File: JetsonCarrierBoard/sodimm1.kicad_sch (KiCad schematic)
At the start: 6 parts

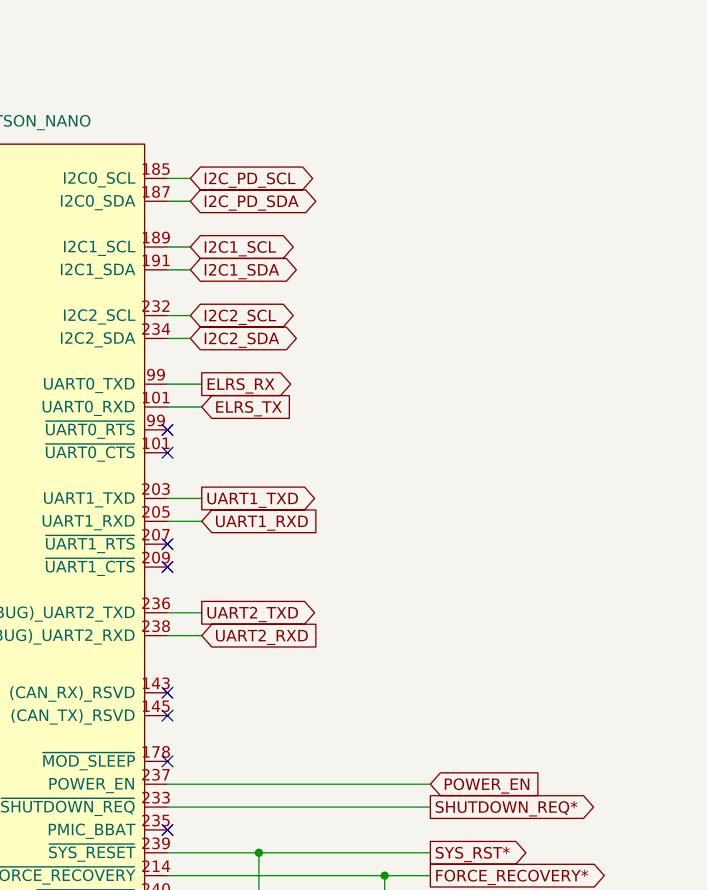
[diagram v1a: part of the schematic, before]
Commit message: Added basic circuits, LED circuit, GPIO pins in GPIO page
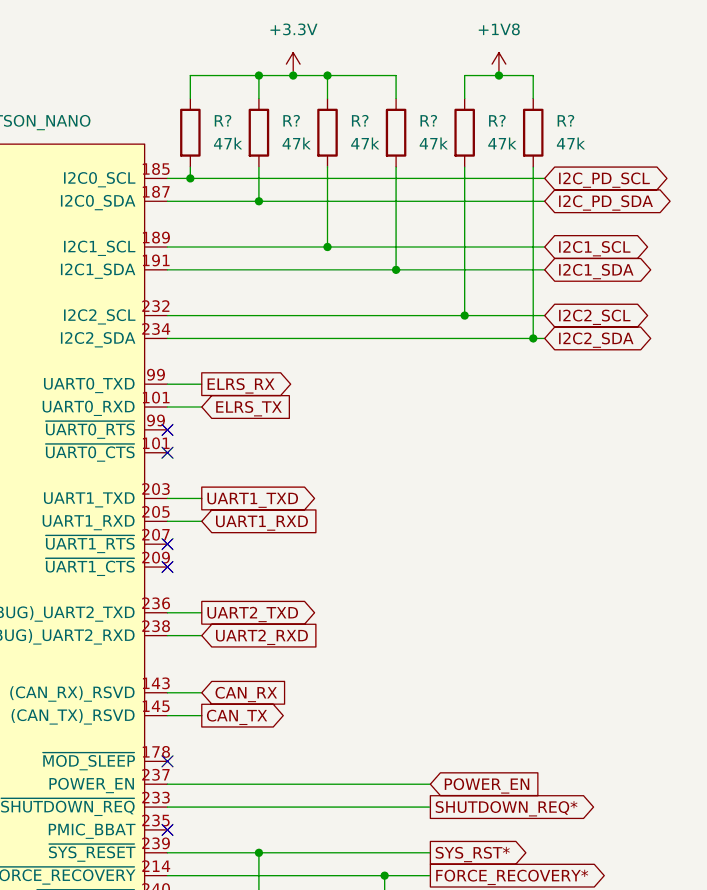
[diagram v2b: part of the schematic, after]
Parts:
- added R? (x6): 47k, symbol Device:R
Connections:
- net I2C1_SCL: now also R?.2
- net I2C1_SDA: now also R?.2
- net I2C2_SCL: now also R?.2
- net I2C2_SDA: now also R?.2
- net I2C_PD_SCL: now also R?.2
- net I2C_PD_SDA: now also R?.2
- net CAN_RX: now reaches J?.143 ((CAN_RX)_RSVD)
- net CAN_TX: now reaches J?.145 ((CAN_TX)_RSVD)
- new net +1V8: R?.1, R?.1
- new net +3.3V: R?.1, R?.1, R?.1, R?.1
- no-connect marks 9 -> 7

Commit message: GPIO wiring
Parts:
- removed R? (x2): 47k, symbol Device:R
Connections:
- net I2C2_SCL: no longer names the net of J?.232 (I2C2_SCL)
- net I2C2_SDA: no longer names the net of J?.234 (I2C2_SDA)
- no-connect marks 7 -> 9
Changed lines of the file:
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@@
   (junction (at 119.38 109.22) (diameter 0) (color 0 0 0 0)
   )
-  (junction (at 204.47 21.59) (diameter 0) (color 0 0 0 0)
-  )
   (junction (at 119.38 43.18) (diameter 0) (color 0 0 0 0)
   )
@@
   )
   (junction (at 119.38 129.54) (diameter 0) (color 0 0 0 0)
-  )
-  (junction (at 200.66 48.26) (diameter 0) (color 0 0 0 0)
-  )
-  (junction (at 208.28 50.8) (diameter 0) (color 0 0 0 0)
   )
   (junction (at 119.38 114.3) (diameter 0) (color 0 0 0 0)
@@
   (no_connect (at 167.64 63.5))
   (no_connect (at 167.64 60.96))
+  (no_connect (at 167.64 50.8))
+  (no_connect (at 167.64 48.26))
   (no_connect (at 167.64 113.03))
   (wire (pts (xy 119.38 124.46) (xy 119.38 127))
@@
     (stroke (width 0) (type default) (color 0 0 0 0))
   )
-  (wire (pts (xy 200.66 24.13) (xy 200.66 21.59))
-    (stroke (width 0) (type default) (color 0 0 0 0))
-  )
   (wire (pts (xy 167.64 55.88) (xy 171.45 55.88))
     (stroke (width 0) (type default) (color 0 0 0 0))
@@
     (stroke (width 0) (type default) (color 0 0 0 0))
   )
-  (wire (pts (xy 208.28 50.8) (xy 208.28 31.75))
-    (stroke (width 0) (type default) (color 0 0 0 0))
-  )
   (wire (pts (xy 119.38 38.1) (xy 119.38 40.64))
     (stroke (width 0) (type default) (color 0 0 0 0))
@@
     (stroke (width 0) (type default) (color 0 0 0 0))
   )
-  (wire (pts (xy 167.64 50.8) (xy 208.28 50.8))
-    (stroke (width 0) (type default) (color 0 0 0 0))
-  )
   (wire (pts (xy 170.18 121.92) (xy 170.18 124.46))
     (stroke (width 0) (type default) (color 0 0 0 0))
@@
     (stroke (width 0) (type default) (color 0 0 0 0))
   )
-  (wire (pts (xy 204.47 21.59) (xy 208.28 21.59))
-    (stroke (width 0) (type default) (color 0 0 0 0))
-  )
   (wire (pts (xy 119.38 147.32) (xy 121.92 147.32))
     (stroke (width 0) (type default) (color 0 0 0 0))
@@
     (stroke (width 0) (type default) (color 0 0 0 0))
   )
-  (wire (pts (xy 167.64 48.26) (xy 200.66 48.26))
-    (stroke (width 0) (type default) (color 0 0 0 0))
-  )
   (wire (pts (xy 119.38 50.8) (xy 119.38 53.34))
     (stroke (width 0) (type default) (color 0 0 0 0))
@@
     (stroke (width 0) (type default) (color 0 0 0 0))
   )
-  (wire (pts (xy 200.66 21.59) (xy 204.47 21.59))
-    (stroke (width 0) (type default) (color 0 0 0 0))
-  )
   (wire (pts (xy 170.18 154.94) (xy 170.18 157.48))
     (stroke (width 0) (type default) (color 0 0 0 0))
@@
     (stroke (width 0) (type default) (color 0 0 0 0))
   )
-  (wire (pts (xy 208.28 21.59) (xy 208.28 24.13))
-    (stroke (width 0) (type default) (color 0 0 0 0))
-  )
   (wire (pts (xy 177.8 35.56) (xy 177.8 31.75))
     (stroke (width 0) (type default) (color 0 0 0 0))
@@
     (stroke (width 0) (type default) (color 0 0 0 0))
   )
-  (wire (pts (xy 200.66 48.26) (xy 200.66 31.75))
-    (stroke (width 0) (type default) (color 0 0 0 0))
-  )
   (wire (pts (xy 119.38 68.58) (xy 119.38 71.12))
     (stroke (width 0) (type default) (color 0 0 0 0))
@@
     (stroke (width 0) (type default) (color 0 0 0 0))
   )
-  (wire (pts (xy 200.66 48.26) (xy 209.55 48.26))
-    (stroke (width 0) (type default) (color 0 0 0 0))
-  )
   (wire (pts (xy 167.64 90.17) (xy 171.45 90.17))
     (stroke (width 0) (type default) (color 0 0 0 0))
@@
     (stroke (width 0) (type default) (color 0 0 0 0))
   )
-  (wire (pts (xy 208.28 50.8) (xy 209.55 50.8))
-    (stroke (width 0) (type default) (color 0 0 0 0))
-  )
   (wire (pts (xy 119.38 134.62) (xy 119.38 137.16))
     (stroke (width 0) (type default) (color 0 0 0 0))
@@
     (effects (font (size 1.27 1.27)) (justify left))
     (property "Intersheet References" "${INTERSHEET_REFS}" (id 0) (at 215.1683 102.7906 0)
-      (effects (font (size 1.27 1.27)) (justify left) hide)
-    )
-  )
-  (global_label "I2C2_SCL" (shape bidirectional) (at 209.55 48.26 0) (fields_autoplaced)
-    (effects (font (size 1.27 1.27)) (justify left))
-    (property "Intersheet References" "${INTERSHEET_REFS}" (id 0) (at 220.7321 48.1806 0)
-      (effects (font (size 1.27 1.27)) (justify left) hide)
-    )
-  )
-  (global_label "I2C2_SDA" (shape bidirectional) (at 209.55 50.8 0) (fields_autoplaced)
-    (effects (font (size 1.27 1.27)) (justify left))
-    (property "Intersheet References" "${INTERSHEET_REFS}" (id 0) (at 220.7926 50.7206 0)
       (effects (font (size 1.27 1.27)) (justify left) hide)
     )
@@
     )
     (pin "1")
-  )
-  (symbol (lib_id "Device:R") (at 208.28 27.94 0) (unit 1)
-    (in_bom yes) (on_board yes) (fields_autoplaced)
-    (property "Reference" "R?" (id 0) (at 210.82 26.6699 0)
-      (effects (font (size 1.27 1.27)) (justify left))
-    )
-    (property "Value" "47k" (id 1) (at 210.82 29.2099 0)
-      (effects (font (size 1.27 1.27)) (justify left))
-    )
-    (property "Footprint" "" (id 2) (at 206.502 27.94 90)
-      (effects (font (size 1.27 1.27)) hide)
-    )
-    (property "Datasheet" "~" (id 3) (at 208.28 27.94 0)
-      (effects (font (size 1.27 1.27)) hide)
-    )
-    (pin "1")
-    (pin "2")
   )
   (symbol (lib_id "Device:D_TVS") (at 191.77 120.65 90) (unit 1)
@@
     (pin "2")
   )
-  (symbol (lib_id "Device:R") (at 200.66 27.94 0) (unit 1)
-    (in_bom yes) (on_board yes) (fields_autoplaced)
-    (property "Reference" "R?" (id 0) (at 203.2 26.6699 0)
-      (effects (font (size 1.27 1.27)) (justify left))
-    )
-    (property "Value" "47k" (id 1) (at 203.2 29.2099 0)
-      (effects (font (size 1.27 1.27)) (justify left))
-    )
-    (property "Footprint" "" (id 2) (at 198.882 27.94 90)
-      (effects (font (size 1.27 1.27)) hide)
-    )
-    (property "Datasheet" "~" (id 3) (at 200.66 27.94 0)
-      (effects (font (size 1.27 1.27)) hide)
-    )
-    (pin "1")
-    (pin "2")
-  )
   (symbol (lib_id "Device:R") (at 177.8 27.94 0) (unit 1)
     (in_bom yes) (on_board yes) (fields_autoplaced)
@@
       (effects (font (size 1.27 1.27)) hide)
     )
-    (pin "1")
-  )
-  (symbol (lib_id "power:+1V8") (at 204.47 21.59 0) (unit 1)
-    (in_bom yes) (on_board yes) (fields_autoplaced)
-    (property "Reference" "#PWR?" (id 0) (at 204.47 25.4 0)
-      (effects (font (size 1.27 1.27)) hide)
-    )
-    (property "Value" "+1V8" (id 1) (at 204.47 16.51 0))
-    (property "Footprint" "" (id 2) (at 204.47 21.59 0)
-      (effects (font (size 1.27 1.27)) hide)
-    )
-    (property "Datasheet" "" (id 3) (at 204.47 21.59 0)
-      (effects (font (size 1.27 1.27)) hide)
-    )

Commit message: Adding more Title block info and changing main hierarchical page layout
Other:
- title: (none) -> SODIMM Connector 1/3
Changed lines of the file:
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@@
 (kicad_sch (version 20211123) (generator eeschema)
   (paper "A4")
+  (title_block
+    (title "SODIMM Connector 1/3")
+    (date "2022-09-18")
+    (rev "1.0")
+  )
   (junction (at 119.38 99.06) (diameter 0) (color 0 0 0 0)
   )

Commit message: Readability improvements mostly
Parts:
- removed C? (x2): 100u, symbol Device:C
- added C? (x2): 330u, symbol Device:C_Polarized
- C?: value 560u -> (none)
- D? (x2): value D_TVS -> (none)
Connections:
- net ELRS_RX is gone; now on net UART0_TXD: J?.99 (~{UART0_RTS})
- net ELRS_TX is gone; now on net UART0_RXD: J?.101 (~{UART0_CTS})
- net +5V: now also C?.1, C?.1
- net GND: now also C?.2, C?.2
- net UART0_RXD: now reaches J?.101 (~{UART0_CTS})
- net UART0_TXD: now reaches J?.99 (~{UART0_RTS})
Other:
- note added: "DEBUG"
- note added: "PD Controller I2C"
